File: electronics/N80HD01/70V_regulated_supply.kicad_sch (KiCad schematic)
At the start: 27 parts, among them Q1 KSC2383YTA, Q2 KSC2383YTA, Q3 KSC2383YTA, Q4 2SC5198, U1 LM741

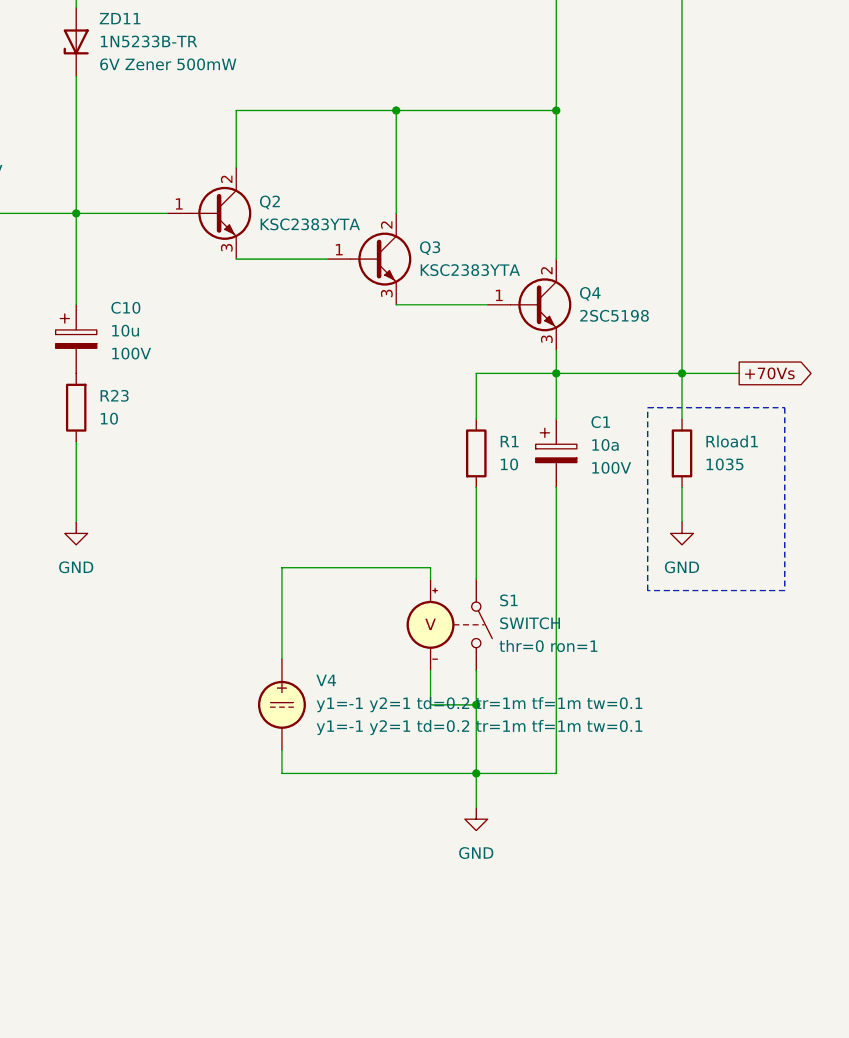
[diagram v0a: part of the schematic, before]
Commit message: Working on 70 Volt supply for HV
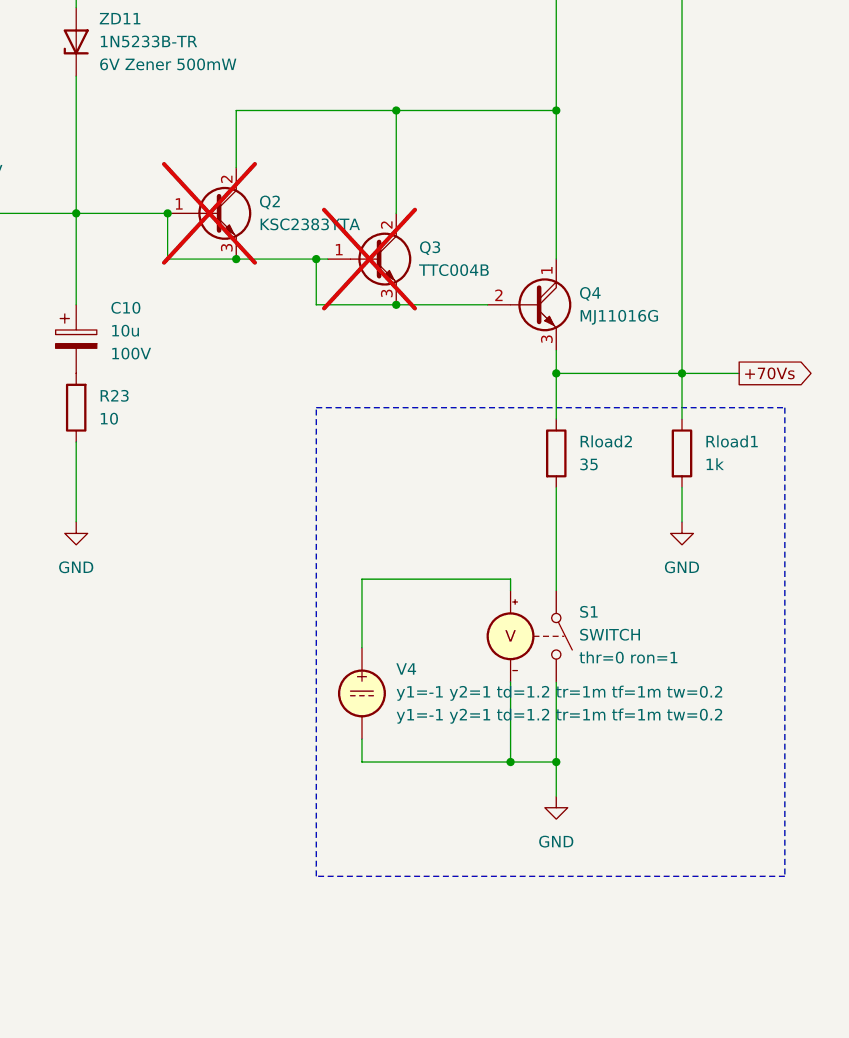
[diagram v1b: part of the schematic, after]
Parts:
- removed C1: 10a, symbol Device:C_Polarized
- Q2: now not fitted; now left out of the parts list
- Q3: value KSC2383YTA -> TTC004B; now not fitted; now left out of the parts list
- Q4: value 2SC5198 -> MJ11016G; footprint (none) -> Package_TO_SOT_THT:TO-3PB-3_Vertical; symbol Transistor_BJT:2SD1047 -> Transistor_BJT:Q_NPN_Darlington_CBE
- Rload1: value 1035 -> 1k
- Rload2: renamed from R1; value 10 -> 35; now left out of the parts list
- S1: now left out of the parts list
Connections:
- net +86V: now also Q4.1 (C); no longer Q4.2 (C)
- net at Q2.3 (E), Q3.1 (B): now also C10.1, Q1.2 (C), Q2.1 (B), Q3.3 (E), Q4.2 (B), R21.1, ZD11.1 (K)
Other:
- moved on the sheet: Rload2, S1, V4
